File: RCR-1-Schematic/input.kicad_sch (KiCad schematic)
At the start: 18 parts

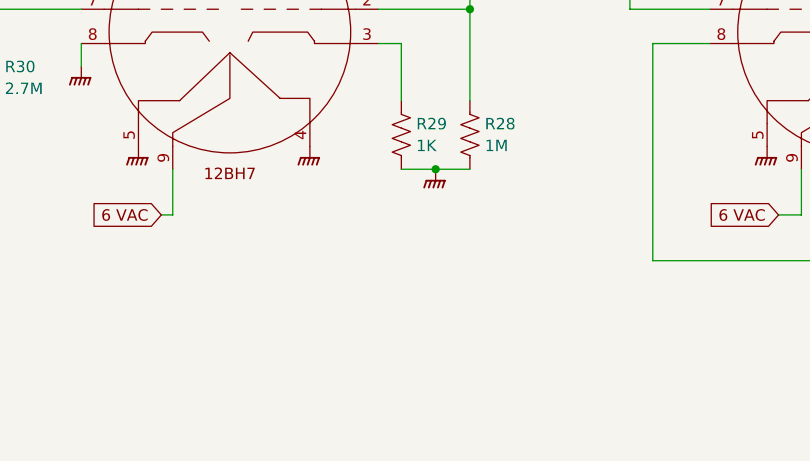
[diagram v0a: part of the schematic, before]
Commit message: Add some oscilloscope screenshots, fixed some mistakes
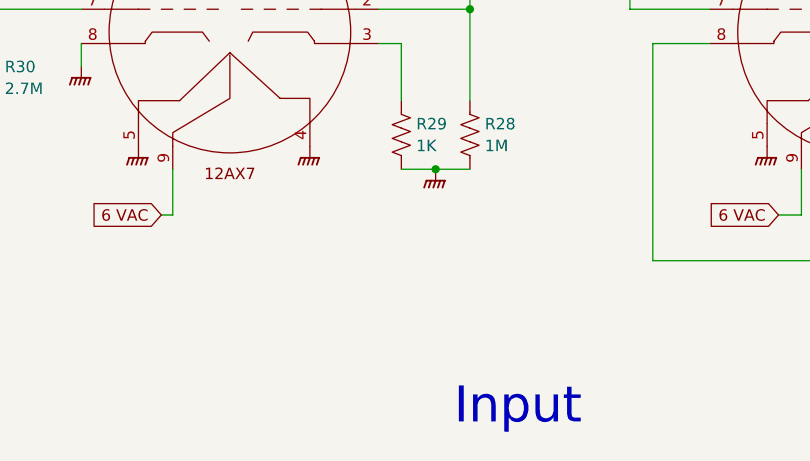
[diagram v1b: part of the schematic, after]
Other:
- note added: "Input"
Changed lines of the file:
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@@
 		(comment 1 "Schematic by Steve Conklin")
+	)
+	(text "Input"
+		(exclude_from_sim no)
+		(at 136.144 140.716 0)
+		(effects
+			(font
+				(size 4 4)
+			)
+		)
 	)
 	(junction
